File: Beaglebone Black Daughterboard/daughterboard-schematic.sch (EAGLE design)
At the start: 9 parts

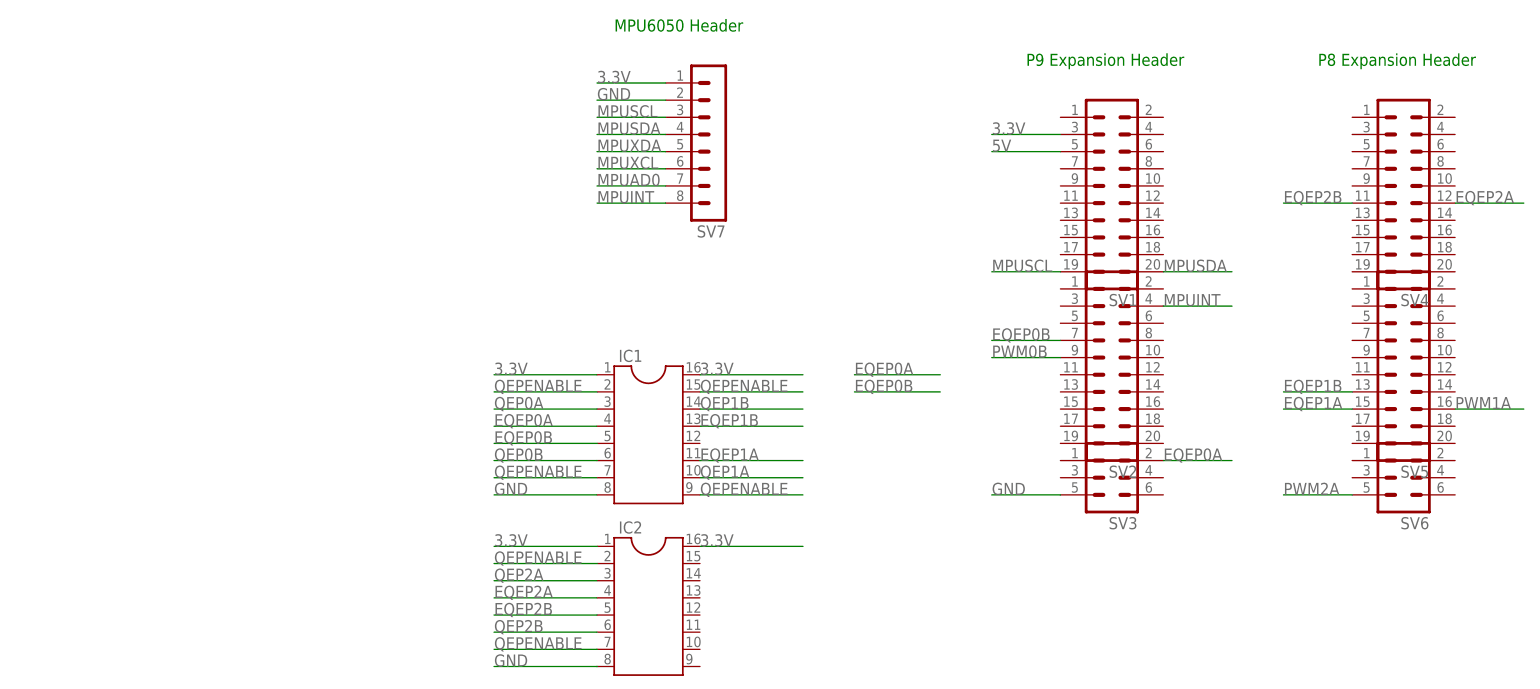
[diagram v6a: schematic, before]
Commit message: PWM and QEP headers added
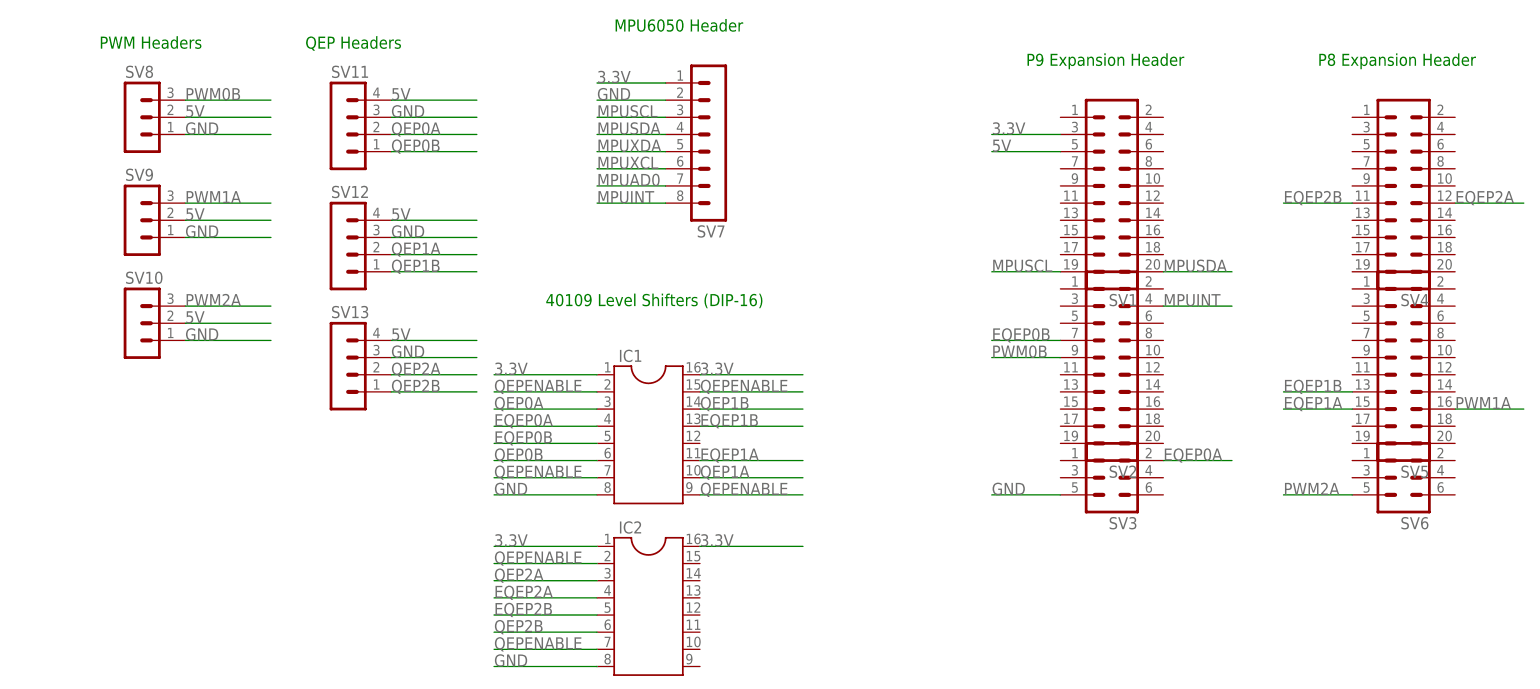
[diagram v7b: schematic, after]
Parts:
- added SV10, SV8, SV9: (no value), con-lstb:MA03-1
- added SV11, SV12, SV13: (no value), con-lstb:MA04-1
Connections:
- net 5V: now also SV10.2, SV11.4, SV12.4, SV13.4, SV8.2, SV9.2
- net GND: now also SV10.1, SV11.3, SV12.3, SV13.3, SV8.1, SV9.1
- net PWM0B: now also SV8.3
- net PWM1A: now also SV9.3
- net PWM2A: now also SV10.3
- net QEP0A: now also SV11.2
- net QEP0B: now also SV11.1
- net QEP1A: now also SV12.2
- net QEP1B: now also SV12.1
- net QEP2A: now also SV13.2
- net QEP2B: now also SV13.1
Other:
- note added: "40109 Level Shifters (DIP-16)"
- note added: "PWM Headers"
- note added: "QEP Headers"
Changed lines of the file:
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@@
 <part name="IC1" library="ic-package" deviceset="DIL16" device=""/>
 <part name="IC2" library="ic-package" deviceset="DIL16" device=""/>
+<part name="SV8" library="con-lstb" deviceset="MA03-1" device=""/>
+<part name="SV9" library="con-lstb" deviceset="MA03-1" device=""/>
+<part name="SV10" library="con-lstb" deviceset="MA03-1" device=""/>
+<part name="SV11" library="con-lstb" deviceset="MA04-1" device=""/>
+<part name="SV12" library="con-lstb" deviceset="MA04-1" device=""/>
+<part name="SV13" library="con-lstb" deviceset="MA04-1" device=""/>
 </parts>
 <sheets>
@@
 <text x="177.8" y="104.14" size="1.778" layer="91">P8 Expansion Header</text>
 <text x="73.66" y="109.22" size="1.778" layer="91">MPU6050 Header</text>
+<text x="-2.54" y="106.68" size="1.778" layer="91">PWM Headers</text>
+<text x="27.94" y="106.68" size="1.778" layer="91">QEP Headers</text>
+<text x="63.5" y="68.58" size="1.778" layer="91">40109 Level Shifters (DIP-16)</text>
 </plain>
 <instances>
@@
 <instance part="IC1" gate="G$1" x="78.74" y="50.8"/>
 <instance part="IC2" gate="G$1" x="78.74" y="25.4"/>
+<instance part="SV8" gate="G$1" x="2.54" y="96.52"/>
+<instance part="SV9" gate="G$1" x="2.54" y="81.28"/>
+<instance part="SV10" gate="G$1" x="2.54" y="66.04"/>
+<instance part="SV11" gate="1" x="33.02" y="96.52"/>
+<instance part="SV12" gate="1" x="33.02" y="78.74"/>
+<instance part="SV13" gate="1" x="33.02" y="60.96"/>
 </instances>
 <busses>
@@
 <label x="129.54" y="91.44" size="1.778" layer="95"/>
 </segment>
+<segment>
+<pinref part="SV8" gate="G$1" pin="2"/>
+<wire x1="10.16" y1="96.52" x2="22.86" y2="96.52" width="0.1524" layer="91"/>
+<label x="10.16" y="96.52" size="1.778" layer="95"/>
+</segment>
+<segment>
+<pinref part="SV9" gate="G$1" pin="2"/>
+<wire x1="10.16" y1="81.28" x2="22.86" y2="81.28" width="0.1524" layer="91"/>
+<label x="10.16" y="81.28" size="1.778" layer="95"/>
+</segment>
+<segment>
+<pinref part="SV10" gate="G$1" pin="2"/>
+<wire x1="10.16" y1="66.04" x2="22.86" y2="66.04" width="0.1524" layer="91"/>
+<label x="10.16" y="66.04" size="1.778" layer="95"/>
+</segment>
+<segment>
+<pinref part="SV11" gate="1" pin="4"/>
+<wire x1="40.64" y1="99.06" x2="53.34" y2="99.06" width="0.1524" layer="91"/>
+<label x="40.64" y="99.06" size="1.778" layer="95"/>
+</segment>
+<segment>
+<pinref part="SV12" gate="1" pin="4"/>
+<wire x1="40.64" y1="81.28" x2="53.34" y2="81.28" width="0.1524" layer="91"/>
+<label x="40.64" y="81.28" size="1.778" layer="95"/>
+</segment>
+<segment>
+<pinref part="SV13" gate="1" pin="4"/>
+<wire x1="40.64" y1="63.5" x2="53.34" y2="63.5" width="0.1524" layer="91"/>
+<label x="40.64" y="63.5" size="1.778" layer="95"/>
+</segment>
 </net>
 <net name="PWM0B" class="0">
@@
 <label x="129.54" y="60.96" size="1.778" layer="95"/>
 </segment>
+<segment>
+<pinref part="SV8" gate="G$1" pin="3"/>
+<wire x1="10.16" y1="99.06" x2="22.86" y2="99.06" width="0.1524" layer="91"/>
+<label x="10.16" y="99.06" size="1.778" layer="95"/>
+</segment>
 </net>
 <net name="PWM1A" class="0">
@@
 <label x="198.12" y="53.34" size="1.778" layer="95"/>
 </segment>
+<segment>
+<pinref part="SV9" gate="G$1" pin="3"/>
+<wire x1="10.16" y1="83.82" x2="22.86" y2="83.82" width="0.1524" layer="91"/>
+<label x="10.16" y="83.82" size="1.778" layer="95"/>
+</segment>
 </net>
 <net name="PWM2A" class="0">
@@
 <label x="172.72" y="40.64" size="1.778" layer="95"/>
 </segment>
+<segment>
+<pinref part="SV10" gate="G$1" pin="3"/>
+<wire x1="10.16" y1="68.58" x2="22.86" y2="68.58" width="0.1524" layer="91"/>
+<label x="10.16" y="68.58" size="1.778" layer="95"/>
+</segment>
 </net>
 <net name="EQEP1A" class="0">
@@
 </segment>
 <segment>
-<wire x1="109.22" y1="55.88" x2="121.92" y2="55.88" width="0.1524" layer="91"/>
-<label x="109.22" y="55.88" size="1.778" layer="95"/>
-</segment>
-<segment>
 <pinref part="IC1" gate="G$1" pin="5"/>
 <wire x1="71.12" y1="48.26" x2="55.88" y2="48.26" width="0.1524" layer="91"/>
@@
 </segment>
 <segment>
-<wire x1="109.22" y1="58.42" x2="121.92" y2="58.42" width="0.1524" layer="91"/>
-<label x="109.22" y="58.42" size="1.778" layer="95"/>
-</segment>
-<segment>
 <pinref part="IC1" gate="G$1" pin="4"/>
 <wire x1="71.12" y1="50.8" x2="55.88" y2="50.8" width="0.1524" layer="91"/>
@@
 <label x="55.88" y="15.24" size="1.778" layer="95"/>
 </segment>
+<segment>
+<pinref part="SV8" gate="G$1" pin="1"/>
+<wire x1="10.16" y1="93.98" x2="22.86" y2="93.98" width="0.1524" layer="91"/>
+<label x="10.16" y="93.98" size="1.778" layer="95"/>
+</segment>
+<segment>
+<pinref part="SV9" gate="G$1" pin="1"/>
+<wire x1="10.16" y1="78.74" x2="22.86" y2="78.74" width="0.1524" layer="91"/>
+<label x="10.16" y="78.74" size="1.778" layer="95"/>
+</segment>
+<segment>
+<pinref part="SV10" gate="G$1" pin="1"/>
+<wire x1="10.16" y1="63.5" x2="22.86" y2="63.5" width="0.1524" layer="91"/>
+<label x="10.16" y="63.5" size="1.778" layer="95"/>
+</segment>
+<segment>
+<pinref part="SV11" gate="1" pin="3"/>
+<wire x1="40.64" y1="96.52" x2="53.34" y2="96.52" width="0.1524" layer="91"/>
+<label x="40.64" y="96.52" size="1.778" layer="95"/>
+</segment>
+<segment>
+<pinref part="SV12" gate="1" pin="3"/>
+<wire x1="40.64" y1="78.74" x2="53.34" y2="78.74" width="0.1524" layer="91"/>
+<label x="40.64" y="78.74" size="1.778" layer="95"/>
+</segment>
+<segment>
+<pinref part="SV13" gate="1" pin="3"/>
+<wire x1="40.64" y1="60.96" x2="53.34" y2="60.96" width="0.1524" layer="91"/>
+<label x="40.64" y="60.96" size="1.778" layer="95"/>
+</segment>
 </net>
 <net name="QEP1A" class="0">
@@
 <label x="86.36" y="43.18" size="1.778" layer="95"/>
 </segment>
+<segment>
+<pinref part="SV12" gate="1" pin="2"/>
+<wire x1="40.64" y1="76.2" x2="53.34" y2="76.2" width="0.1524" layer="91"/>
+<label x="40.64" y="76.2" size="1.778" layer="95"/>
+</segment>
 </net>
 <net name="QEP1B" class="0">
@@
 <label x="86.36" y="53.34" size="1.778" layer="95"/>
 </segment>
+<segment>
+<pinref part="SV12" gate="1" pin="1"/>
+<wire x1="40.64" y1="73.66" x2="53.34" y2="73.66" width="0.1524" layer="91"/>
+<label x="40.64" y="73.66" size="1.778" layer="95"/>
+</segment>
 </net>
 <net name="QEP0B" class="0">
@@
 <label x="55.88" y="45.72" size="1.778" layer="95"/>
 </segment>
+<segment>
+<pinref part="SV11" gate="1" pin="1"/>
+<wire x1="40.64" y1="91.44" x2="53.34" y2="91.44" width="0.1524" layer="91"/>
+<label x="40.64" y="91.44" size="1.778" layer="95"/>
+</segment>
 </net>
 <net name="QEP0A" class="0">
@@
 <label x="55.88" y="53.34" size="1.778" layer="95"/>
 </segment>
+<segment>
+<pinref part="SV11" gate="1" pin="2"/>
+<wire x1="40.64" y1="93.98" x2="53.34" y2="93.98" width="0.1524" layer="91"/>
+<label x="40.64" y="93.98" size="1.778" layer="95"/>
+</segment>
 </net>
 <net name="QEP2A" class="0">
@@
 <label x="55.88" y="27.94" size="1.778" layer="95"/>
 </segment>
+<segment>
+<pinref part="SV13" gate="1" pin="2"/>
+<wire x1="40.64" y1="58.42" x2="53.34" y2="58.42" width="0.1524" layer="91"/>
+<label x="40.64" y="58.42" size="1.778" layer="95"/>
+</segment>
 </net>
 <net name="QEP2B" class="0">
@@
 <label x="55.88" y="20.32" size="1.778" layer="95"/>
 </segment>
-</net>
+<segment>
+<pinref part="SV13" gate="1" pin="1"/>
+<wire x1="40.64" y1="55.88" x2="53.34" y2="55.88" width="0.1524" layer="91"/>
+<label x="40.64" y="55.88" size="1.778" layer="95"/>
+</segment>
+</net>

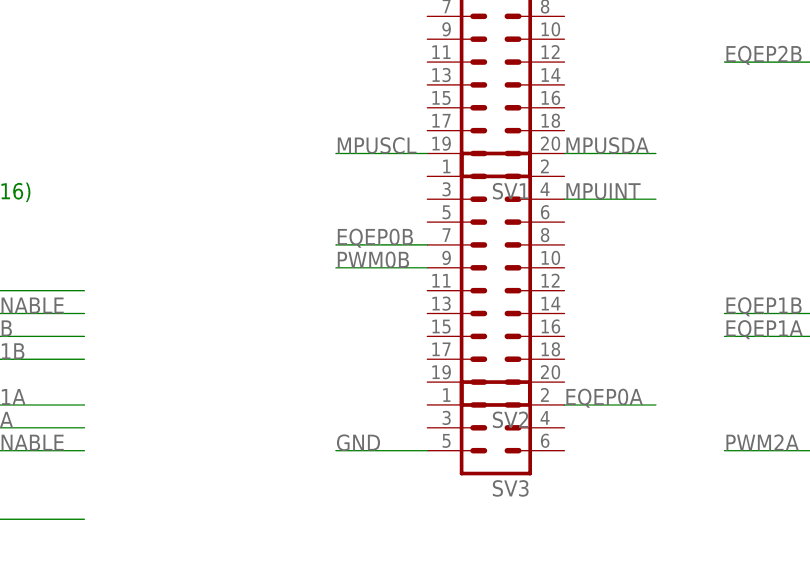
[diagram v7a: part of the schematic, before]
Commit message: Add qepenable to cape
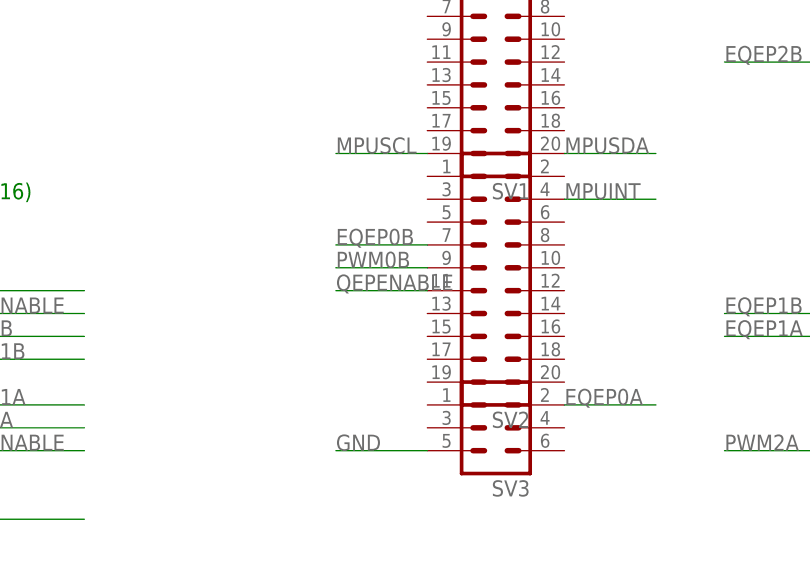
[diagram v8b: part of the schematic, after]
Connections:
- net QEPENABLE: now also SV2.11
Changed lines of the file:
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@@
 <label x="55.88" y="17.78" size="1.778" layer="95"/>
+</segment>
+<segment>
+<pinref part="SV2" gate="1" pin="11"/>
+<wire x1="139.7" y1="58.42" x2="129.54" y2="58.42" width="0.1524" layer="91"/>
+<label x="129.54" y="58.42" size="1.778" layer="95"/>
 </segment>
 </net>
